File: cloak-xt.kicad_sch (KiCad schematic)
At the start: 43 parts, among them J1 JST, J2 Conn_01x02, J3 Conn_01x04, U1 STM32F072CBT6

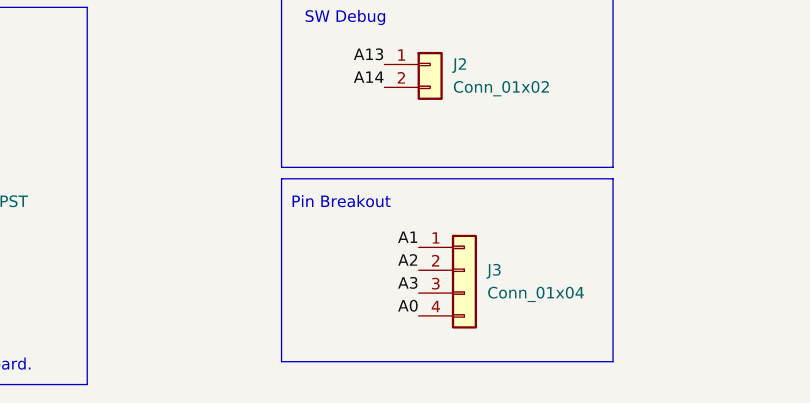
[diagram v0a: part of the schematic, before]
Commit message: Add spacebar 6.25u/2.25u/2.75u and remove 6u/3u/3u
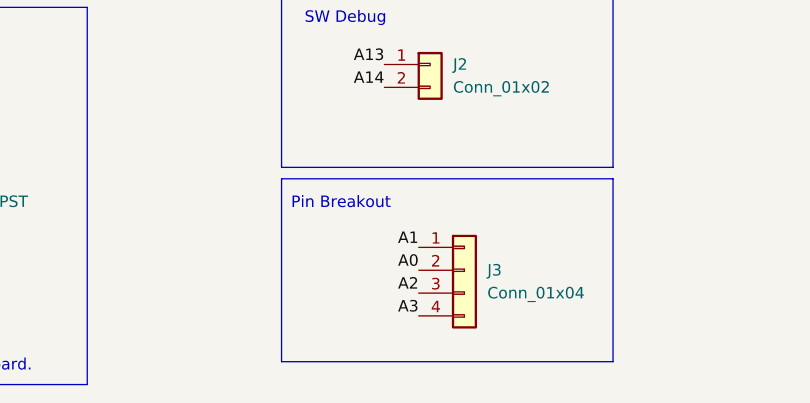
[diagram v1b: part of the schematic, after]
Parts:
- J2: footprint Connector_PinHeader_1.00mm:PinHeader_1x02_P1.00mm_Vertical -> Connector_PinHeader_1.27mm:PinHeader_1x02_P1.27mm_Vertical
- J3: footprint Connector_PinHeader_1.00mm:PinHeader_1x04_P1.00mm_Vertical -> Connector_PinHeader_1.27mm:PinHeader_1x04_P1.27mm_Vertical
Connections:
- net A0: now also J3.2 (Pin_2); no longer J3.4 (Pin_4)
- net A2: now also J3.3 (Pin_3); no longer J3.2 (Pin_2)
- net A3: now also J3.4 (Pin_4); no longer J3.3 (Pin_3)
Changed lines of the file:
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@@
 	)
 	(label "A0"
-		(at 250.19 153.67 180)
+		(at 250.19 148.59 180)
 		(fields_autoplaced yes)
 		(effects
@@
 	)
 	(label "A3"
-		(at 250.19 151.13 180)
+		(at 250.19 153.67 180)
 		(fields_autoplaced yes)
 		(effects
@@
 	)
 	(label "A2"
-		(at 250.19 148.59 180)
+		(at 250.19 151.13 180)
 		(fields_autoplaced yes)
 		(effects
@@
 			)
 		)
-		(property "Footprint" "Connector_PinHeader_1.00mm:PinHeader_1x04_P1.00mm_Vertical"
+		(property "Footprint" "Connector_PinHeader_1.27mm:PinHeader_1x04_P1.27mm_Vertical"
 			(at 255.27 148.59 0)
 			(effects
@@
 			)
 		)
-		(property "Footprint" "Connector_PinHeader_1.00mm:PinHeader_1x02_P1.00mm_Vertical"
+		(property "Footprint" "Connector_PinHeader_1.27mm:PinHeader_1x02_P1.27mm_Vertical"
 			(at 251.46 125.73 0)
 			(effects
